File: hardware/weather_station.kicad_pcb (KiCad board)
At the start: 2 copper layers, 70 parts, among them J1 USB_MICRO, Q1 BD135, Q2 BD135, SW1 SWITCH_SPDT, U1 nRF51x22, U2 TMP112, U3 BMP280, U4 Si7013, U5 LM3668, U6 MCP73831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

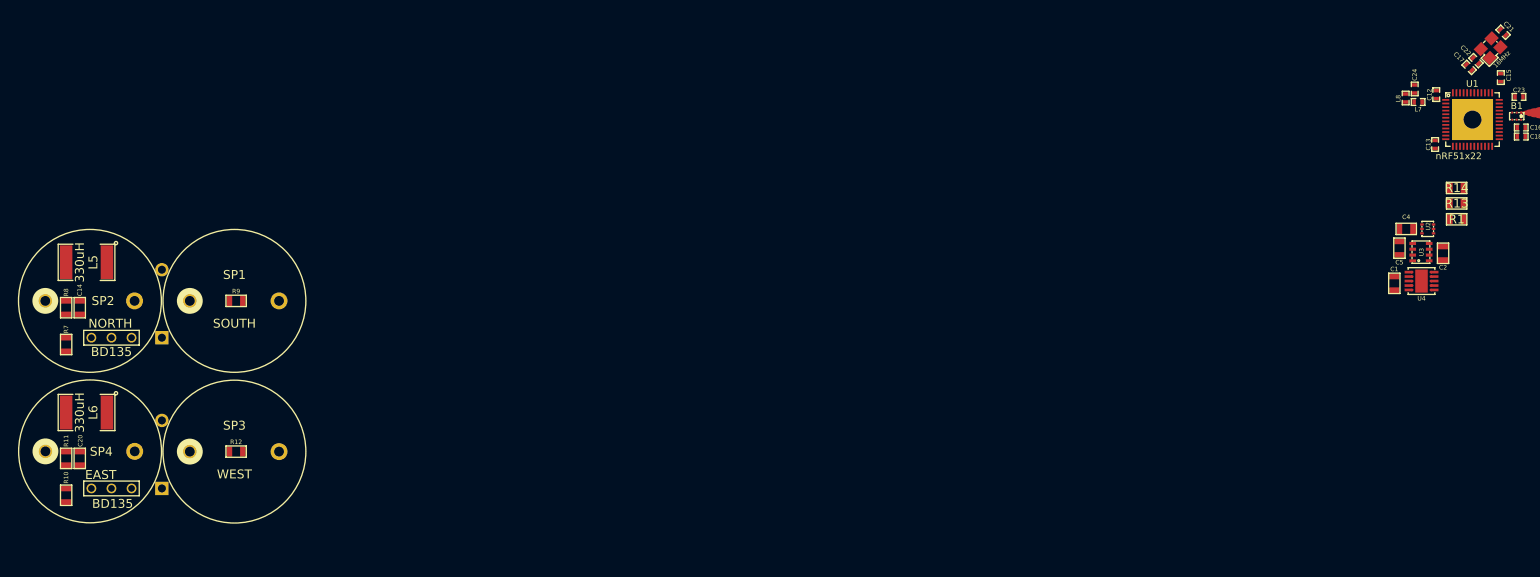
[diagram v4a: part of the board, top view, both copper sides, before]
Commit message: Group the ultrasonic circuitry, the MCU circuitry and the TWI circuitry together
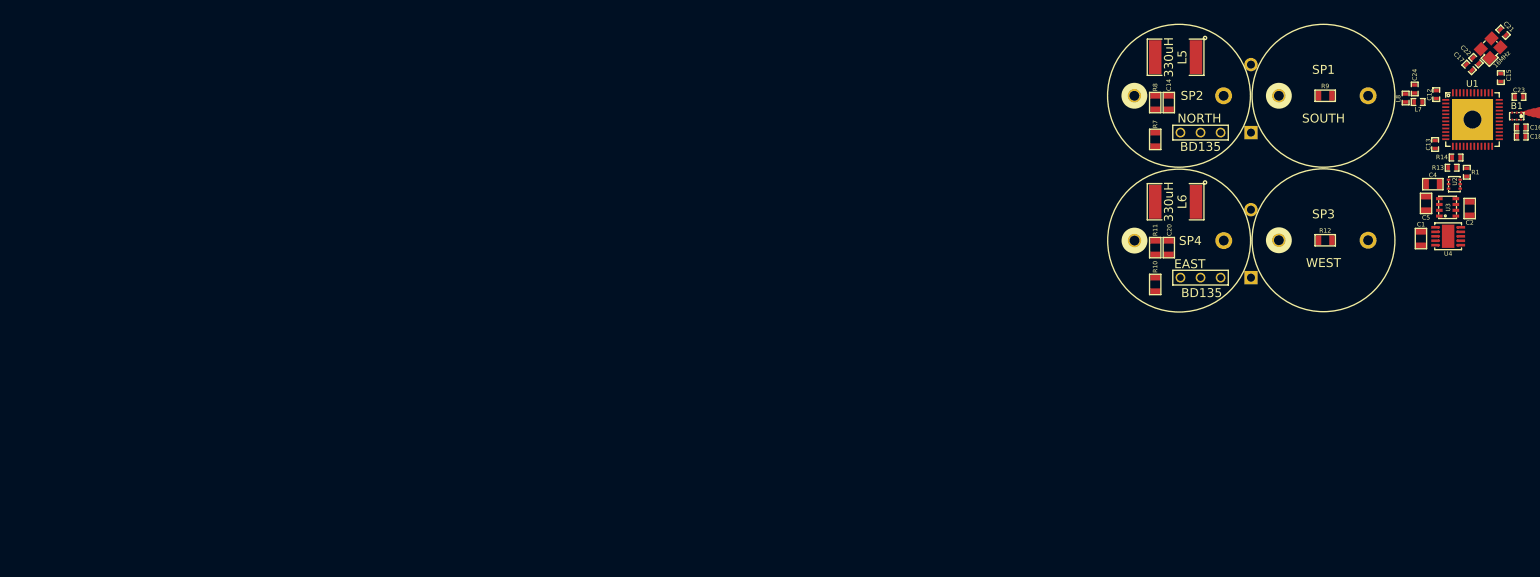
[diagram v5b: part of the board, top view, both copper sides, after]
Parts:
- R1, R13, R14: footprint SMD_Packages:SMD-0603 -> SMD_Packages:SMD-0402
- moved R12 124.3 mm to (231.0, 55.1)
- moved SP3 124.3 mm to (230.8, 55.1)
- moved D4 124.3 mm to (222.7, 55.4)
- moved Q2 124.3 mm to (217.0, 59.2)
- moved L6 124.3 mm to (214.2, 50.7)
- moved SP4 124.3 mm to (214.6, 55.1)
- moved C20 124.3 mm to (213.5, 55.9)
- moved R10 124.3 mm to (212.0, 60.0)
- moved R11 124.3 mm to (212.0, 55.9)
- moved D3 124.2 mm to (222.7, 39.2)
- moved Q1 124.2 mm to (217.0, 43.0)
- moved L5 124.2 mm to (214.2, 34.5)
- moved R7 124.2 mm to (212.0, 43.8)
- moved R9 124.2 mm to (231.0, 38.9)
- moved C14 124.2 mm to (213.5, 39.6)
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
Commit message: Update layout
Group rest of components together, route all components together except the GND
rail and the 3.3V rail.
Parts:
- added REF** (x2): muwave_arcstub, muwave_arcstub, F.Cu at (0.00, 0.00)
- moved C7 91.9 mm to (200.3, 57.4), turned to 180 degrees
- moved U7 87.7 mm to (200.4, 59.8), turned to 270 degrees
- moved C10 85.9 mm to (206.6, 49.7)
- moved C3 85.9 mm to (200.3, 55.1)
- moved C8 85.9 mm to (200.3, 49.0)
- moved L1 85.9 mm to (195.8, 51.9)
- moved R4 85.9 mm to (203.1, 49.0)
- moved U5 85.9 mm to (200.3, 52.0)
- moved L3 85.9 mm to (204.9, 49.0)
- moved R6 84.7 mm to (199.6, 63.9)
- moved L4 84.6 mm to (201.4, 63.9)
- moved C19 84.5 mm to (203.2, 64.6)
- moved BT1 83.8 mm to (190.4, 44.0)
- moved C9 83.8 mm to (184.3, 47.1)
- moved D2 83.8 mm to (180.2, 46.9)
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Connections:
- U1 pad 14: SCL -> SDA
- U1 pad 15: SDA -> SCL
- U1 pad 3: Net-(U1-Pad3) -> PULSE1
- U1 pad 4: V50_EN -> PWM1
- U1 pad 5: PWM1 -> V50_EN
- U1 pad 7: PULSE1 -> PULSE2
- U1 pad 8: PULSE2 -> Net-(U1-Pad8)
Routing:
- net V5.0: track 0.00 -> 177.2 mm
- net PULSE2: track 0.00 -> 104.9 mm
- net VIN: track 0.00 -> 81.2 mm
- net Net-(D4-Pad1): track 0.00 -> 65.4 mm
- net PULSE1: track 0.00 -> 64.4 mm
- net VBAT: track 0.00 -> 54.6 mm
- net V50_EN: track 0.00 -> 53.3 mm, vias 0 -> 2
- net Net-(C8-Pad1): track 0.00 -> 50.6 mm
- net PWM2: track 0.00 -> 35.8 mm
- net Net-(D3-Pad1): track 0.00 -> 34.9 mm
- net PWM1: track 0.00 -> 34.8 mm
- net AVDD: track 0.00 -> 33.5 mm, vias 0 -> 2
- net Net-(C11-Pad1): track 0.00 -> 24.7 mm
- net Net-(C6-Pad1): track 0.00 -> 14.5 mm
- net Net-(Q1-Pad3): track 0.00 -> 14.2 mm
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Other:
- rule via_min_drill: 0.1778 -> 0.3302
- rule via_min_size: 0.3302 -> 0.508

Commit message: Add board outline
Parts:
- removed REF** (x2): muwave_arcstub, muwave_arcstub
- moved D1 2.09 mm to (180.2, 43.2), turned to 180 degrees
- moved R5 1.14 mm to (181.2, 40.6)
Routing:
- net Net-(C6-Pad1): track 14.5 -> 18.3 mm
- net Net-(D1-Pad2): track 3.12 -> 2.35 mm
- net Net-(R5-Pad2): track 1.34 -> 1.87 mm
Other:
- board outline added: 85.4 x 36.4 mm
- copper layers 2 -> 4

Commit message: Finish routing the board
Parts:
- moved C11 1.55 mm to (198.3, 62.6), turned to 180 degrees
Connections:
- U1 pad : (no net) -> GND
- U5 pad ~: (no net) -> GND
- U7 pad ~: (no net) -> GND
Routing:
- net GND: track 0.00 -> 195.0 mm, vias 0 -> 115
- net V3.3: track 9.71 -> 53.9 mm, vias 0 -> 19
- net V5.0: track 177.2 -> 179.5 mm
- added copper zone on In1.Cu, net GND
- added copper zone on In2.Cu, net GND
- added copper zone on B.Cu, net V3.3
- added copper zone on F.Cu, net V3.3
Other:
- outline, holes or cut-outs redrawn
- board text added: "GND - SGND"
